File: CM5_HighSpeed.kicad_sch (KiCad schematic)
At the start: 5 parts, among them J10 690-019-298-412, U18 RT9742SNGV

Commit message: change cad data
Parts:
- C136: renamed from C114; footprint Capacitor_SMD:C_0402_1005Metric -> Capacitor_SMD:C_0402_1005Metric_Pad0.74x0.62mm_HandSolder
- C141: renamed from C115; footprint Capacitor_SMD:C_0402_1005Metric -> Capacitor_SMD:C_0402_1005Metric_Pad0.74x0.62mm_HandSolder
- renumbered U18 to U19
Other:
- moved on the sheet: C136, C141, J10

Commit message: change clearance
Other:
- company: Copyright © 2024 Raspberry Pi Ltd. -> (none)
- title: Compute Module 5 IO Board - CM5 - Highspeed -> (none)
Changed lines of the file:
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@@
 	(paper "A4")
 	(title_block
-		(title "Compute Module 5 IO Board - CM5 - Highspeed")
 		(rev "1")
-		(company "Copyright © 2024 Raspberry Pi Ltd.")
-		(comment 1 "www.raspberrypi.com")
 	)
 	(junction

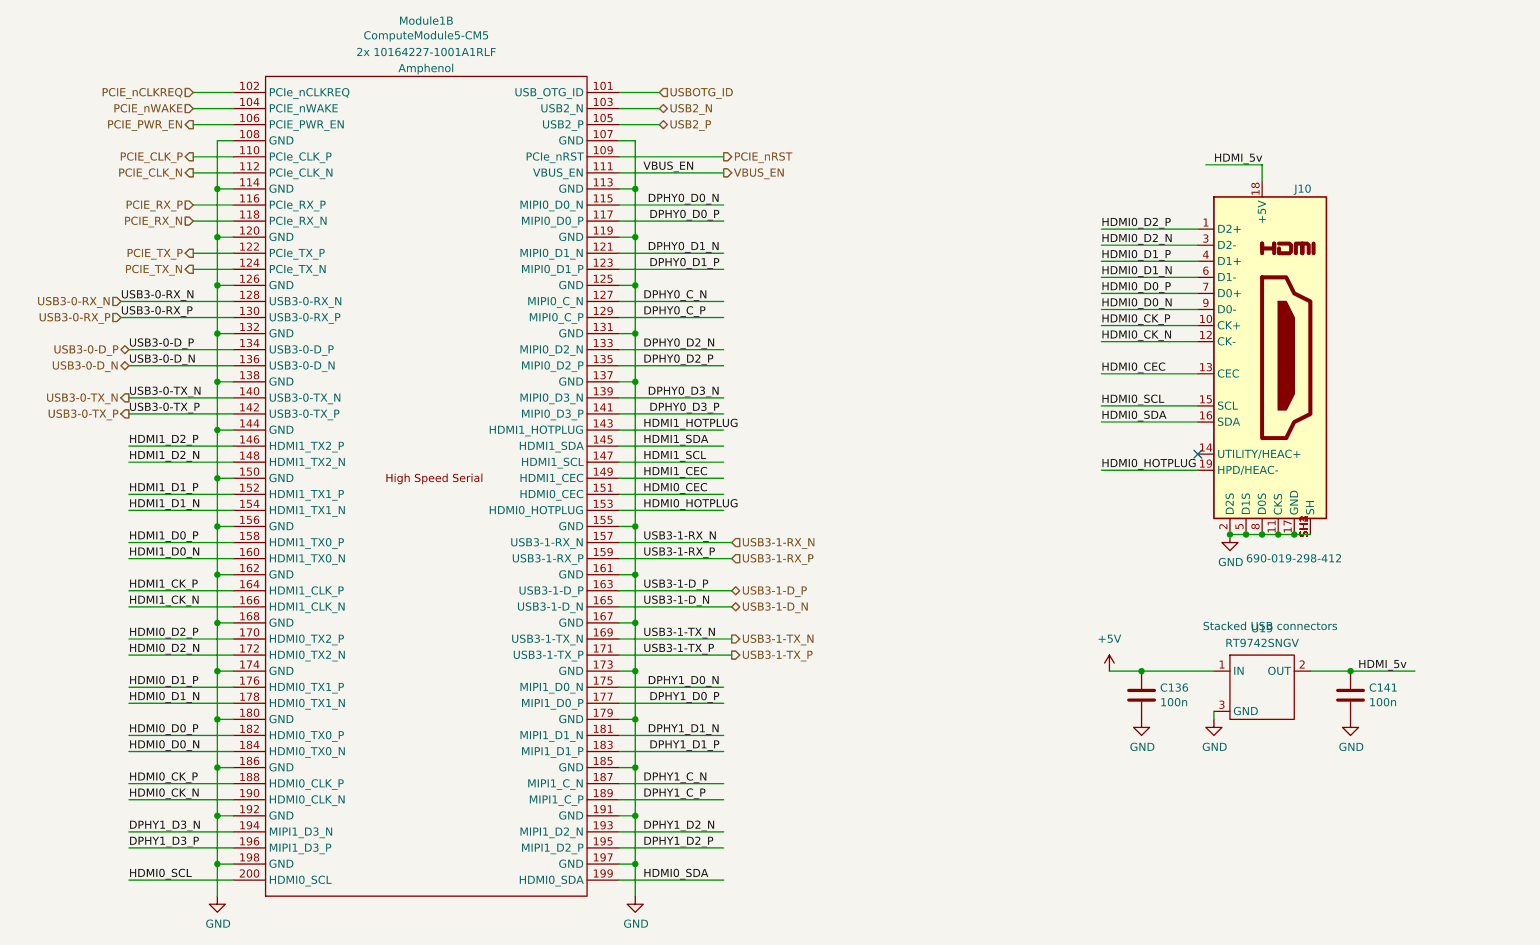
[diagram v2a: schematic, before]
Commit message: remove efuse
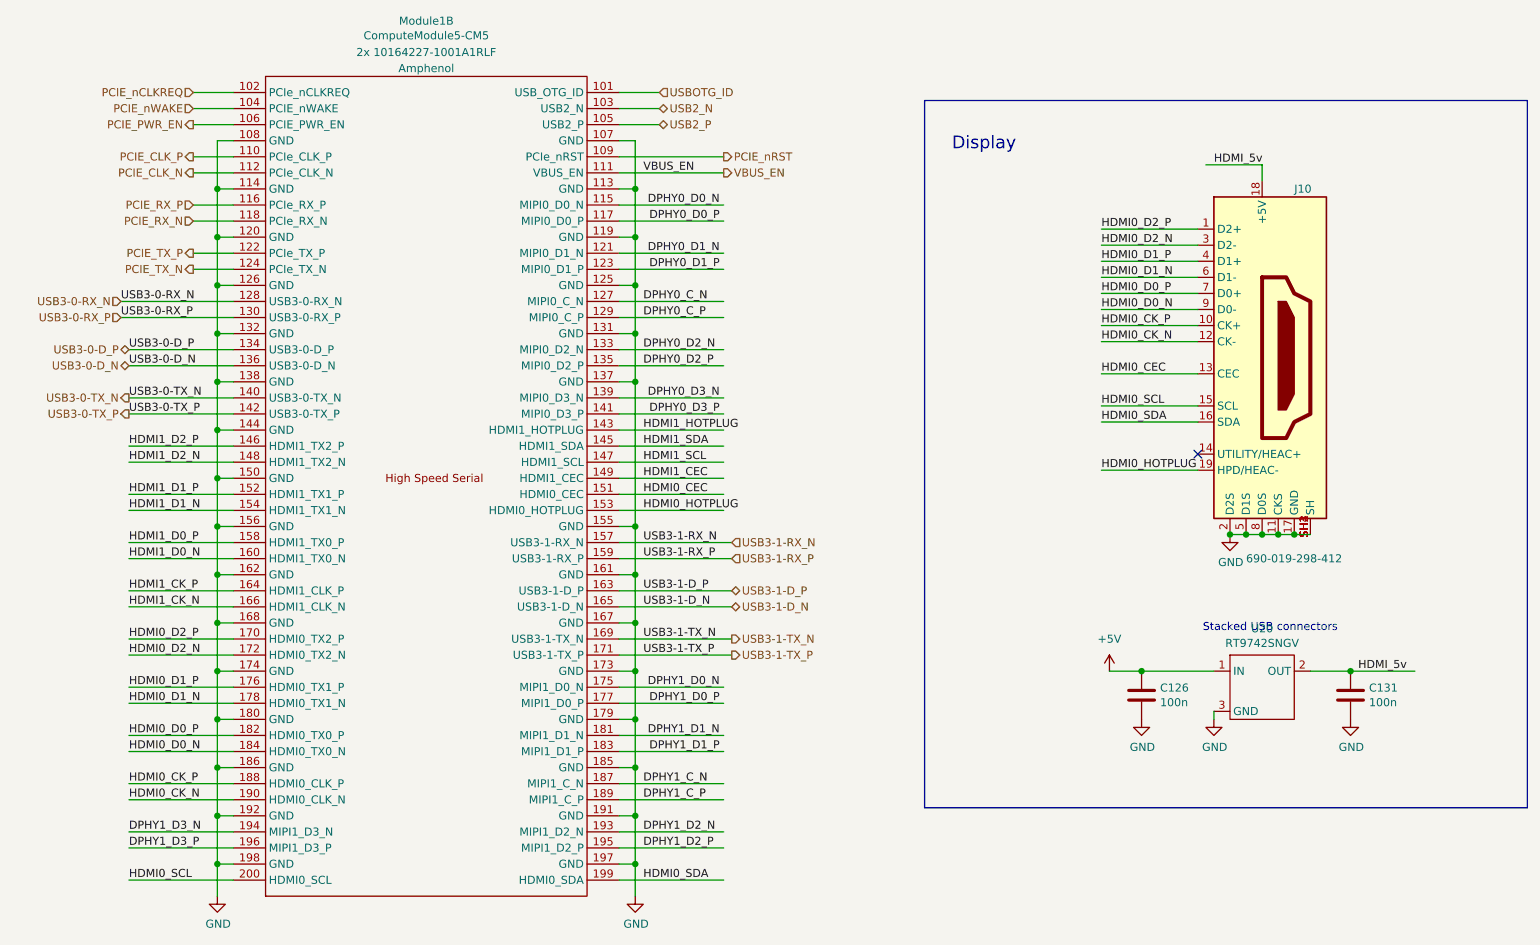
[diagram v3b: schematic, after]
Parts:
- renumbered C136 to C126, C141 to C131, U19 to U20
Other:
- note added: "Display"
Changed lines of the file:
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@@
+		)
+	)
+	(rectangle
+		(start 166.37 44.45)
+		(end 261.62 156.21)
+		(stroke
+			(width 0)
+			(type default)
+		)
+		(fill
+			(type none)
 		)
 	)
@@
 			)
 			(justify right bottom)
+		)
+	)
+	(text "Display"
+		(exclude_from_sim no)
+		(at 175.768 51.308 0)
+		(effects
+			(font
+				(size 2.007 2.007)
+			)
 		)
 	)
@@
 		(on_board yes)
 		(dnp no)
-		(property "Reference" "C141"
+		(property "Reference" "C131"
 			(at 236.601 137.2616 0)
 			(effects
@@
 			(project "CM5IO"
 				(path "/dd07ab80-a59c-44f4-ac7d-849e21e1384e/5e5501ac-41c8-4cac-b3fc-c2c46c035d54"
-					(reference "C141")
+					(reference "C131")
 					(unit 1)
 				)
@@
 		(on_board yes)
 		(dnp no)
-		(property "Reference" "C136"
+		(property "Reference" "C126"
 			(at 203.581 137.2616 0)
 			(effects
@@
 			(project "CM5IO"
 				(path "/dd07ab80-a59c-44f4-ac7d-849e21e1384e/5e5501ac-41c8-4cac-b3fc-c2c46c035d54"
-					(reference "C136")
+					(reference "C126")
 					(unit 1)
 				)
@@
 		(on_board yes)
 		(dnp no)
-		(property "Reference" "U19"
+		(property "Reference" "U20"
 			(at 219.71 127.889 0)
 			(effects
@@
 			(project "CM5IO"
 				(path "/dd07ab80-a59c-44f4-ac7d-849e21e1384e/5e5501ac-41c8-4cac-b3fc-c2c46c035d54"
-					(reference "U19")
+					(reference "U20")
 					(unit 1)
 				)

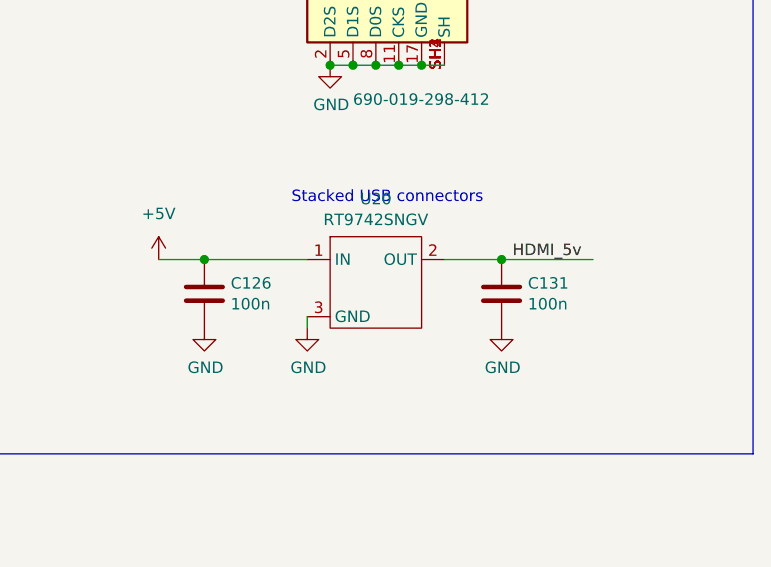
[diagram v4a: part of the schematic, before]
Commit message: add sata capacitor
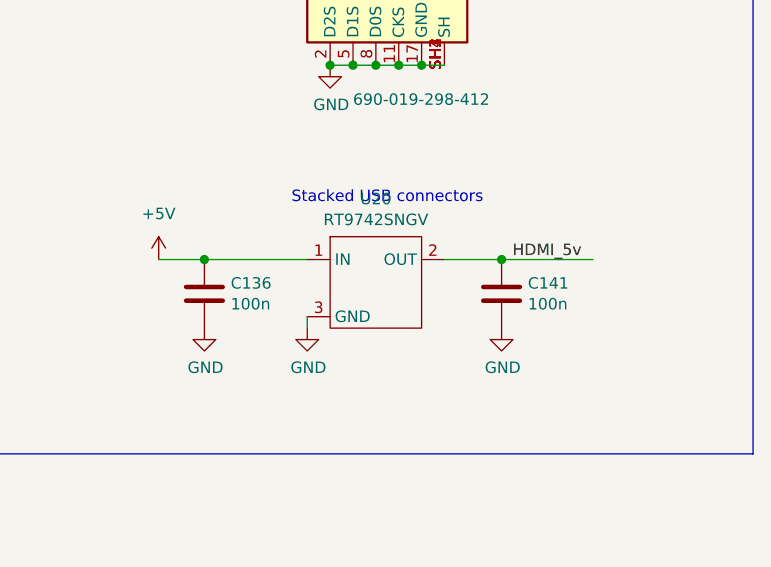
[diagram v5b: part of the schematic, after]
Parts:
- renumbered C126 to C136, C131 to C141

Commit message: add logo
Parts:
- Module1: value ComputeModule5-CM5 -> Compute Module 5
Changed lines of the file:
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@@
 			)
 		)
-		(property "Value" "ComputeModule5-CM5"
+		(property "Value" "Compute Module 5"
 			(at 87.63 34.1884 0)
 			(effects

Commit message: end route
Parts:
- renumbered C136 to C109, C141 to C110, J10 to J11, U20 to U18
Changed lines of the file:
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@@
 		(on_board yes)
 		(dnp no)
-		(property "Reference" "J10"
+		(property "Reference" "J11"
 			(at 224.79 58.42 0)
 			(effects
@@
 			(project "CM5IO"
 				(path "/dd07ab80-a59c-44f4-ac7d-849e21e1384e/5e5501ac-41c8-4cac-b3fc-c2c46c035d54"
-					(reference "J10")
+					(reference "J11")
 					(unit 1)
 				)
@@
 		(on_board yes)
 		(dnp no)
-		(property "Reference" "C141"
+		(property "Reference" "C110"
 			(at 236.601 137.2616 0)
 			(effects
@@
 			(project "CM5IO"
 				(path "/dd07ab80-a59c-44f4-ac7d-849e21e1384e/5e5501ac-41c8-4cac-b3fc-c2c46c035d54"
-					(reference "C141")
+					(reference "C110")
 					(unit 1)
 				)
@@
 		(on_board yes)
 		(dnp no)
-		(property "Reference" "C136"
+		(property "Reference" "C109"
 			(at 203.581 137.2616 0)
 			(effects
@@
 			(project "CM5IO"
 				(path "/dd07ab80-a59c-44f4-ac7d-849e21e1384e/5e5501ac-41c8-4cac-b3fc-c2c46c035d54"
-					(reference "C136")
+					(reference "C109")
 					(unit 1)
 				)
@@
 		(on_board yes)
 		(dnp no)
-		(property "Reference" "U20"
+		(property "Reference" "U18"
 			(at 219.71 127.889 0)
 			(effects
@@
 			(project "CM5IO"
 				(path "/dd07ab80-a59c-44f4-ac7d-849e21e1384e/5e5501ac-41c8-4cac-b3fc-c2c46c035d54"
-					(reference "U20")
-					(unit 1)
-				)
+					(reference "U18")
+					(unit 1)
+				)
